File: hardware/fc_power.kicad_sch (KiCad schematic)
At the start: 42 parts, among them U27 TLV75533PDQNR, U3 LMR51430YFDDCR, U4 LMR51430YFDDCR, U6 LP5912-1.8DRVR, U7 LP5912-3.3DRVR

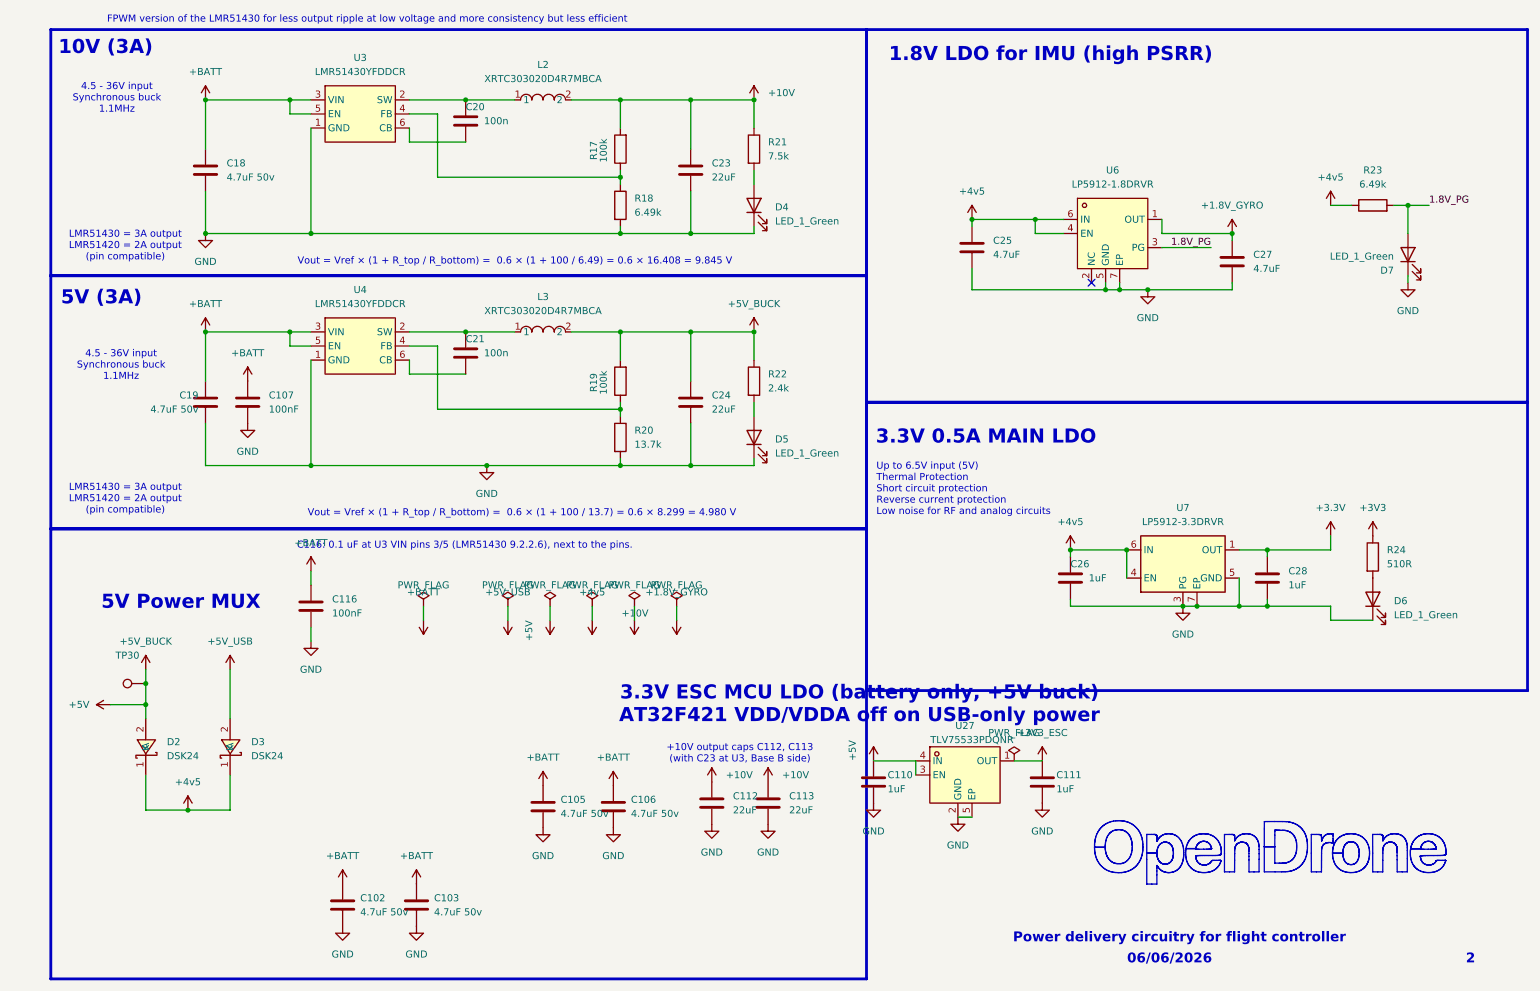
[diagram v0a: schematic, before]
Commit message: One board from the owner's 2026-08-22 Base and Core, BMP580 baro (#26)
The board is rebuilt from d81e559 (the hand-routed Base recovered from KiCad
local history and the hand-routed Core of 1fe3d21) plus the always-on +10V of
9aba717, instead of the agent-reworked 8fa8d7b. Both layouts sit side by side
in hardware/OpenAIO.kicad_pcb with all routing kept (2513 tracks, 1577 vias),
on the OpenAIO-Whoop 8L HDI stackup.

- Schematic: Core_Interface (J90/J91 LGA) removed; U26 BMP580 + C107/C108 on
  I2C0 at 0x47 (Betaflight BMP5xx default). Netlist otherwise identical to
  9aba717; ERC 31 errors, the 9aba717 baseline.
- Board: Base netclasses and severities; rule area "Core layout" keeps the
  Core's 0.09 line standard. DRC: 3 errors (USB1 peg), 37 unconnected (links).
- lib.pretty footprints replaced by the board instances; BMP580 imported with
  easyeda2kicad (LCSC C22391138).
- Not carried from 8fa8d7b: TXU0101 LED-strip buffer, +3V3_ESC, SWD pads,
  DFM edits; firmware ISSUES I2/I3 reopened.
- Docs: README pinout re-measured, AGENTS.md, research/ROUTING.md, Betaflight
  target USE_BARO_BMP580.

Co-authored-by: Stan <stan@openaio.local>
Co-authored-by: Claude Opus 5.5 <noreply@anthropic.com>
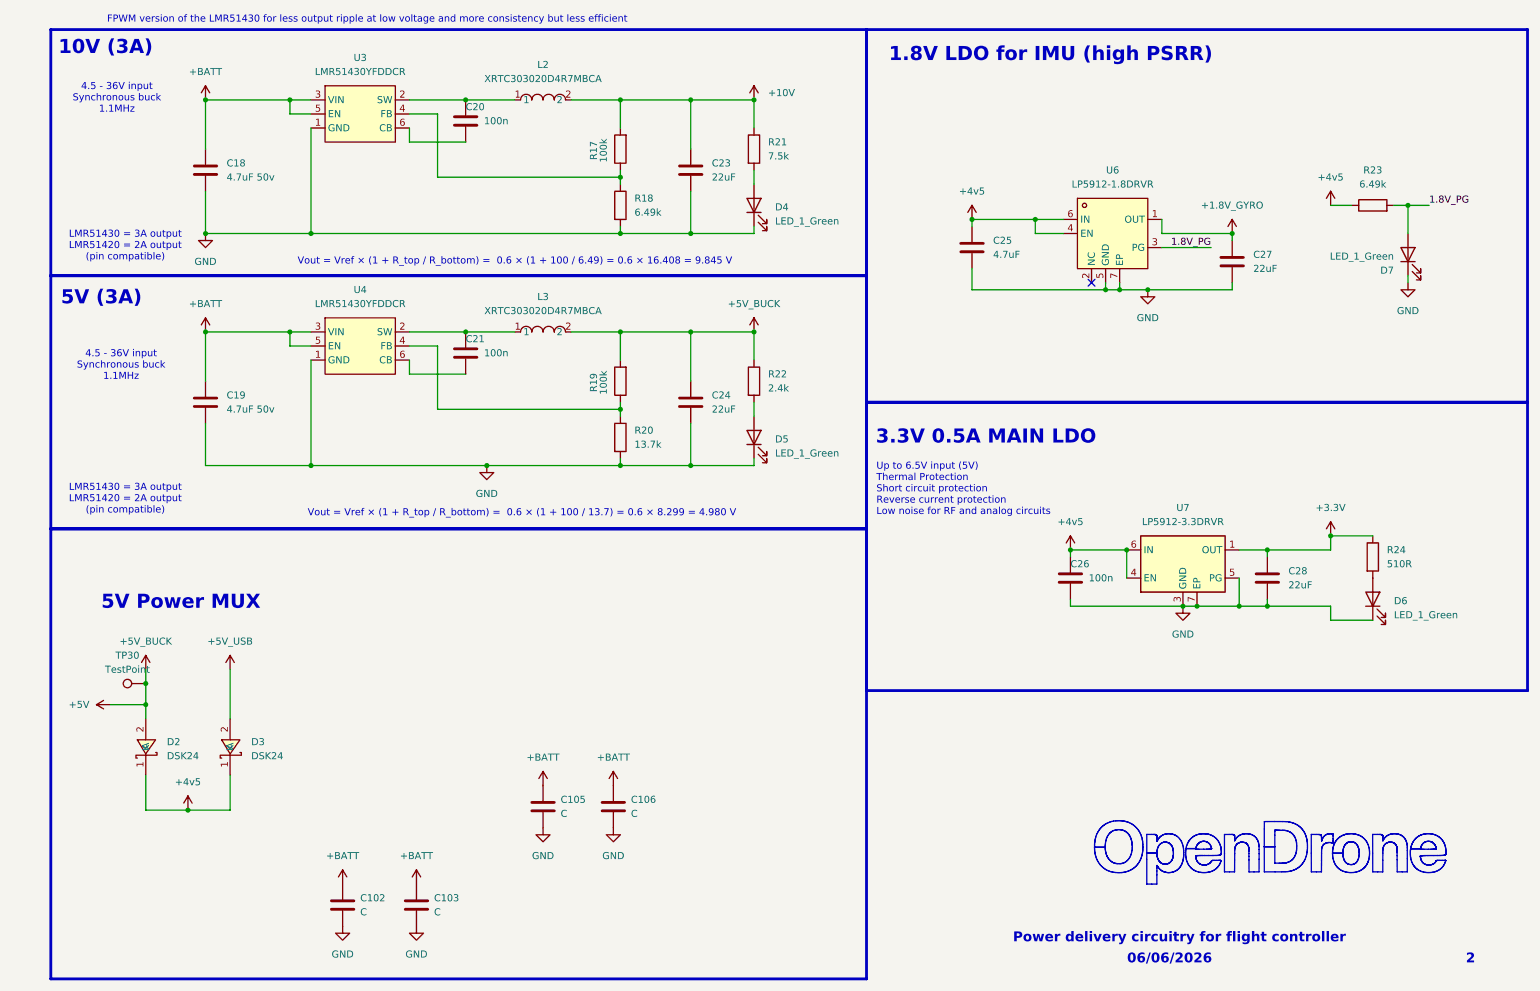
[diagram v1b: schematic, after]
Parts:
- removed C107, C116: 100nF, lib:C_0402_1005Metric, symbol Device:C
- removed C110, C111: 1uF, lib:C_0201_0603Metric, symbol Device:C
- removed C112, C113: 22uF, lib:C_0603_1608Metric, symbol Device:C
- removed U27: TLV75533PDQNR, lib:X2SON-4_L1.0-W1.0-P0.65-TL-EP, symbol lib:TLV75533PDQNR
- C102, C103: value 4.7uF 50v -> C; LCSC C98192 -> (none); MPN CL21A475KBQNNNE -> (none); Manufacturer Samsung Electro-Mechanics -> (none)
- C105, C106: value 4.7uF 50v -> C; LCSC C380366 -> (none); MPN TCC1206X7R475K500HT -> (none); Manufacturer CCTC -> (none)
- C26: value 1uF -> 100n; footprint lib:C_0402_1005Metric -> lib:C_0201_0603Metric; LCSC C52923 -> C76939; MPN CL05A105KA5NQNC -> GRM033R61E104KE14D; Manufacturer Samsung Electro-Mechanics -> Murata Electronics
- C27: value 4.7uF -> 22uF; LCSC C23733 -> C415703; MPN CL05A475MP5NRNC -> GRM155R60J226ME11D; Manufacturer Samsung Electro-Mechanics -> Murata
- C28: value 1uF -> 22uF; LCSC C52923 -> C415703; MPN CL05A105KA5NQNC -> GRM155R60J226ME11D; Manufacturer Samsung Electro-Mechanics -> Murata
- D4, D5, D6, D7: MPN XL-1005UGC -> XL-1005UGC
- R18, R23: MPN AF0201FR-076K49L -> (none); Manufacturer YAGEO -> (none)
- R21: MPN RC0201FR-077K5L -> (none); Manufacturer YAGEO -> (none)
- R22: MPN RTT012401FTH -> (none); Manufacturer RALEC -> (none)
- R24: MPN RC0201FR-07510RL -> (none); Manufacturer YAGEO -> (none)
- U7: symbol lib:LP5912-3.3DRV_1 -> lib:LP5912-3.3DRV_1_OpenAIO
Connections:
- net +3V3 is gone; now on net +3.3V: R24.1
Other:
- note removed: "+10V output caps C112, C113 (with C23 at U3, Base B side)"
- note removed: "3.3V ESC MCU LDO (battery only, +5V buck) AT32F421 VDD/VDDA off on USB-only power"
- note removed: "C116: 0.1 uF at U3 VIN pins 3/5 (LMR51430 9.2.2.6), next to the pins."
- title: Power -> (none)

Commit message: Library: every symbol, footprint and 3D model project-local (#28)
* Owner: board cleanup, Core placed on the board

Co-Authored-By: Claude Opus 5.5 <noreply@anthropic.com>

* Library: every symbol, footprint and 3D model project-local

- 3D models: 275 board model paths and 28 lib.pretty footprints pointed at
  KiCad's stock install or at ${OPENDRONE_LIB} (which this machine's KiCad sets
  to a path that does not exist, so 9 models were missing). All now resolve to
  ${KIPRJMOD}/lib.3dshapes; the three missing ones come from the repo's
  KiCad-Library submodule. .wrl replaced by the .step sibling where one exists.
- Symbols: the 14 stock symbols (Device, power, Connector, Connector_Generic,
  MCU_Espressif) copied into lib.kicad_sym from the schematic's own cache and
  relinked as lib:. Four lib symbols refreshed from the schematic (they still
  held the 8fa8d7b copies).
- Pruned: 11 unused footprints, 7 unused symbols, unreferenced model files.
- tools/localise_models.py and tools/localise_symbols.py keep it that way.
- Checks: board diff is model lines only; netlist identical; ERC 31 errors as
  before, lib_symbol_mismatch 9 -> 0.

Co-Authored-By: Claude Opus 5.5 <noreply@anthropic.com>

---------

Co-authored-by: Stan <stan@openaio.local>
Co-authored-by: Claude Opus 5.5 <noreply@anthropic.com>
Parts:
- C102, C103, C105, C106, C18, C19, C20, C21, C23, C24, C25, C26, C27, C28: symbol Device:C -> lib:C
- D4, D5, D6, D7: symbol Device:LED -> lib:LED
- R17, R18, R19, R20, R21, R22, R23, R24: symbol Device:R -> lib:R
- TP30: symbol Connector:TestPoint -> lib:TestPoint
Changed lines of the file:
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@@
 	)
 	(symbol
-		(lib_id "power:+5V")
+		(lib_id "lib:+5V")
 		(at 46.355 140.97 0)
 		(unit 1)
@@
 	)
 	(symbol
-		(lib_id "Device:LED")
+		(lib_id "lib:LED")
 		(at 259.08 66.04 90)
 		(unit 1)
@@
 	)
 	(symbol
-		(lib_id "Device:R")
+		(lib_id "lib:R")
 		(at 116.84 88.9 180)
 		(unit 1)
@@
 	)
 	(symbol
-		(lib_id "Device:C")
+		(lib_id "lib:C")
 		(at 129.54 50.8 0)
 		(unit 1)
@@
 	)
 	(symbol
-		(lib_id "power:+5V")
+		(lib_id "lib:+5V")
 		(at 24.765 147.32 90)
 		(unit 1)
@@
 	)
 	(symbol
-		(lib_id "Device:C")
+		(lib_id "lib:C")
 		(at 102.87 165.735 0)
 		(unit 1)
@@
 	)
 	(symbol
-		(lib_id "power:GND")
+		(lib_id "lib:GND")
 		(at 41.91 62.23 0)
 		(unit 1)
@@
 	)
 	(symbol
-		(lib_id "Device:R")
+		(lib_id "lib:R")
 		(at 252.73 57.15 90)
 		(unit 1)
@@
 	)
 	(symbol
-		(lib_id "Device:C")
+		(lib_id "lib:C")
 		(at 41.91 50.8 0)
 		(unit 1)
@@
 	)
 	(symbol
-		(lib_id "power:GND")
+		(lib_id "lib:GND")
 		(at 212.09 72.39 0)
 		(unit 1)
@@
 	)
 	(symbol
-		(lib_id "power:GND")
+		(lib_id "lib:GND")
 		(at 102.87 169.545 0)
 		(unit 1)
@@
 	)
 	(symbol
-		(lib_id "Device:C")
+		(lib_id "lib:C")
 		(at 66.675 183.515 0)
 		(unit 1)
@@
 	)
 	(symbol
-		(lib_id "power:+5V")
+		(lib_id "lib:+5V")
 		(at 245.11 57.15 0)
 		(unit 1)
@@
 	)
 	(symbol
-		(lib_id "power:GND")
+		(lib_id "lib:GND")
 		(at 259.08 71.12 0)
 		(unit 1)
@@
 	)
 	(symbol
-		(lib_id "Device:LED")
+		(lib_id "lib:LED")
 		(at 140.97 99.06 90)
 		(unit 1)
@@
 	)
 	(symbol
-		(lib_id "power:GND")
+		(lib_id "lib:GND")
 		(at 218.44 129.54 0)
 		(unit 1)
@@
 	)
 	(symbol
-		(lib_id "power:+3.3V")
+		(lib_id "lib:+3.3V")
 		(at 245.11 116.84 0)
 		(unit 1)
@@
 	)
 	(symbol
-		(lib_id "power:+5V")
+		(lib_id "lib:+5V")
 		(at 38.735 166.37 0)
 		(unit 1)
@@
 	)
 	(symbol
-		(lib_id "power:+3.3V")
+		(lib_id "lib:+3.3V")
 		(at 227.33 62.23 0)
 		(unit 1)
@@
 	)
 	(symbol
-		(lib_id "power:+12V")
+		(lib_id "lib:+12V")
 		(at 140.97 38.1 0)
 		(unit 1)
@@
 	)
 	(symbol
-		(lib_id "Device:R")
+		(lib_id "lib:R")
 		(at 116.84 99.06 0)
 		(unit 1)
@@
 	)
 	(symbol
-		(lib_id "Device:C")
+		(lib_id "lib:C")
 		(at 198.12 124.46 0)
 		(unit 1)
@@
 	)
 	(symbol
-		(lib_id "Device:LED")
+		(lib_id "lib:LED")
 		(at 252.73 128.27 90)
 		(unit 1)
@@
 	)
 	(symbol
-		(lib_id "power:+5V")
+		(lib_id "lib:+5V")
 		(at 31.115 140.97 0)
 		(unit 1)
@@
 	)
 	(symbol
-		(lib_id "power:GND")
+		(lib_id "lib:GND")
 		(at 115.57 169.545 0)
 		(unit 1)
@@
 	)
 	(symbol
-		(lib_id "power:GND")
+		(lib_id "lib:GND")
 		(at 80.01 187.325 0)
 		(unit 1)
@@
 	)
 	(symbol
-		(lib_id "Device:C")
+		(lib_id "lib:C")
 		(at 88.9 83.82 0)
 		(unit 1)
@@
 	)
 	(symbol
-		(lib_id "Device:C")
+		(lib_id "lib:C")
 		(at 115.57 165.735 0)
 		(unit 1)
@@
 	)
 	(symbol
-		(lib_id "power:+BATT")
+		(lib_id "lib:+BATT")
 		(at 80.01 179.705 0)
 		(unit 1)
@@
 	)
 	(symbol
-		(lib_id "Device:C")
+		(lib_id "lib:C")
 		(at 80.01 183.515 0)
 		(unit 1)
@@
 	)
 	(symbol
-		(lib_id "power:+BATT")
+		(lib_id "lib:+BATT")
 		(at 115.57 161.925 0)
 		(unit 1)
@@
 	)
 	(symbol
-		(lib_id "Connector:TestPoint")
+		(lib_id "lib:TestPoint")
 		(at 31.115 143.51 90)
 		(unit 1)
@@
 	)
 	(symbol
-		(lib_id "Device:C")
+		(lib_id "lib:C")
 		(at 180.34 64.77 0)
 		(unit 1)
@@
 	)
 	(symbol
-		(lib_id "Device:C")
+		(lib_id "lib:C")
 		(at 227.33 67.31 0)
 		(unit 1)
@@
 	)
 	(symbol
-		(lib_id "power:+BATT")
+		(lib_id "lib:+BATT")
 		(at 41.91 80.01 0)
 		(unit 1)
@@
 	)
 	(symbol
-		(lib_id "Device:C")
+		(lib_id "lib:C")
 		(at 88.9 41.91 0)
 		(unit 1)
@@
 	)
 	(symbol
-		(lib_id "Device:R")
+		(lib_id "lib:R")
 		(at 116.84 46.99 180)
 		(unit 1)
@@
 	)
 	(symbol
-		(lib_id "power:+5V")
+		(lib_id "lib:+5V")
 		(at 180.34 59.69 0)
 		(unit 1)
@@
 	)
 	(symbol
-		(lib_id "Device:R")
+		(lib_id "lib:R")
 		(at 140.97 88.9 0)
 		(unit 1)
@@
 	)
 	(symbol
-		(lib_id "power:GND")
+		(lib_id "lib:GND")
 		(at 92.71 104.14 0)
 		(unit 1)
@@
 	)
 	(symbol
-		(lib_id "Device:C")
+		(lib_id "lib:C")
 		(at 233.68 124.46 0)
 		(unit 1)
@@
 	)
 	(symbol
-		(lib_id "Device:R")
+		(lib_id "lib:R")
 		(at 116.84 57.15 0)
 		(unit 1)
@@
 	)
 	(symbol
-		(lib_id "Device:R")
+		(lib_id "lib:R")
 		(at 140.97 46.99 0)
 		(unit 1)
@@
 	)
 	(symbol
-		(lib_id "power:+5V")
+		(lib_id "lib:+5V")
 		(at 140.97 80.01 0)
 		(unit 1)
@@
 	)
 	(symbol
-		(lib_id "power:+BATT")
+		(lib_id "lib:+BATT")
 		(at 66.675 179.705 0)
 		(unit 1)
@@
 	)
 	(symbol
-		(lib_id "power:+BATT")
+		(lib_id "lib:+BATT")
 		(at 102.87 161.925 0)
 		(unit 1)
@@
 	)
 	(symbol
-		(lib_id "Device:C")
+		(lib_id "lib:C")
 		(at 129.54 92.71 0)
 		(unit 1)
@@
 	)
 	(symbol
-		(lib_id "Device:C")
+		(lib_id "lib:C")
 		(at 41.91 92.71 0)
 		(unit 1)
@@
 	)
 	(symbol
-		(lib_id "power:+5V")
+		(lib_id "lib:+5V")
 		(at 198.12 119.38 0)
 		(unit 1)
@@
 	)
 	(symbol
-		(lib_id "Device:LED")
+		(lib_id "lib:LED")
 		(at 140.97 57.15 90)
 		(unit 1)
@@
 	)
 	(symbol
-		(lib_id "power:GND")
+		(lib_id "lib:GND")
 		(at 66.675 187.325 0)
 		(unit 1)
@@
 	)
 	(symbol
-		(lib_id "power:+BATT")
+		(lib_id "lib:+BATT")
 		(at 41.91 38.1 0)
 		(unit 1)
@@
 	)
 	(symbol
-		(lib_id "Device:R")
+		(lib_id "lib:R")
 		(at 252.73 120.65 0)
 		(unit 1)

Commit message: One 3.3 V rail: U7 becomes TLV76733DRVR (1 A), U23 removed
- U7 LP5912-3.3DRVR (500 mA) -> TLV76733DRVR (1 A, LCSC C2848334, as on
  OpenESC-20x20), same WSON-6 2x2 land; SNS (pin 2) tied to OUT in the
  schematic and by a 0.25 mm jumper on B.Cu.
- U23 TLV75533 removed; the 17 +3V3 power symbols are +3.3V, and the board's
  +3V3 copper (24 tracks, 6 vias, 3 pours) moved onto +3.3V.
- Netlist: only U7 (value, MPN, LCSC, pin 2), U23 gone, +3V3 merged into +3.3V.
  ERC 31 errors as before. DRC: no new unconnected beyond the link the old
  +3V3 side now needs to U7.
- Docs: ROUTING.md rails and reroute step; firmware notes on the single rail
  (ISSUES I15 resolved).

Co-Authored-By: Claude Opus 5.5 <noreply@anthropic.com>
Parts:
- U7: value LP5912-3.3DRVR -> TLV76733DRVR; symbol lib:LP5912-3.3DRV_1_OpenAIO -> lib:TLV76733DRVR; LCSC C524780 -> C2848334; MPN LP5912-3.3DRVR -> TLV76733DRVR
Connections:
- net +3.3V: now also U7.2 (SNS)
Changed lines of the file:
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@@
+	(wire
+		(pts
+			(xy 226.06 121.92) (xy 228.6 121.92)
+		)
+		(stroke
+			(width 0)
+			(type default)
+		)
+	)
 	(wire
 		(pts
@@
 		(pts
 			(xy 180.34 60.96) (xy 180.34 59.69)
+		)
+		(stroke
+			(width 0)
+			(type default)
+		)
+	)
+	(wire
+		(pts
+			(xy 228.6 121.92) (xy 228.6 119.38)
 		)
 		(stroke
@@
 	)
 	(symbol
-		(lib_id "lib:LP5912-3.3DRV_1_OpenAIO")
+		(lib_id "lib:TLV76733DRVR")
 		(at 218.44 121.92 0)
 		(unit 1)
@@
 			)
 		)
-		(property "Value" "LP5912-3.3DRVR"
+		(property "Value" "TLV76733DRVR"
 			(at 218.44 114.3 0)
 			(show_name no)
@@
 			)
 		)
-		(property "Datasheet" "http://www.ti.com/lit/ds/symlink/lp5912.pdf"
+		(property "Datasheet" "https://www.ti.com/lit/ds/symlink/tlv767.pdf"
 			(at 218.44 109.22 0)
 			(hide yes)
@@
 			)
 		)
-		(property "Description" "500-mA Ultra-Low-Noise Low-IQ LDO, 3.3V, WSON-6"
+		(property "Description" "1-A, 16-V precision LDO, 3.3 V fixed, WSON-6 2x2; SNS tied to OUT"
 			(at 218.44 121.92 0)
 			(hide yes)
@@
 			)
 		)
-		(property "LCSC" "C524780"
+		(property "LCSC" "C2848334"
 			(at 218.44 121.92 0)
 			(hide yes)
@@
 			)
 		)
-		(property "MPN" "LP5912-3.3DRVR"
+		(property "MPN" "TLV76733DRVR"
 			(at 0 15.24 0)
 			(hide yes)
